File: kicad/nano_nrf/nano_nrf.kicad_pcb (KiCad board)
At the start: 2 copper layers, 50 x 50 mm, 6 parts, among them P1 Digital, P2 Analog, P3 CONN_02X04, P4 CONN_1, P5 CONN_1, P6 CONN_1

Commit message: Leds
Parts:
- added D1: LED, LEDs:LED-5MM, F.Cu at (130.8, 95.2)
- added D2: LED, LEDs:LED-5MM, F.Cu at (162.6, 95.2)
- added D3: LED_RCBG, LEDs:LED-RGB-5MM_Common_Cathode, F.Cu at (143.5, 69.8)
- added R1: 100R, Resistors_ThroughHole:Resistor_Horizontal_RM10mm, F.Cu at (129.5, 88.9)
- added R2: 100R, Resistors_ThroughHole:Resistor_Horizontal_RM10mm, F.Cu at (149.9, 88.9)
- added R3: 180R, Resistors_ThroughHole:Resistor_Horizontal_RM10mm, F.Cu at (133.3, 88.9)
- added R4: 100R, Resistors_ThroughHole:Resistor_Horizontal_RM10mm, F.Cu at (146.1, 88.9)
- added R5: 100R, Resistors_ThroughHole:Resistor_Horizontal_RM10mm, F.Cu at (142.2, 88.9)
- P3: moved to F.Cu
- P4, P5: value CONN_1 -> CONN_01X06; footprint Socket_Arduino_Nano:1pin_Nano -> Socket_Strips:Socket_Strip_Straight_1x06
- moved P5 40.5 mm to (121.9, 88.9), turned to 90 degrees
- moved P4 18.0 mm to (121.9, 106.7), turned to 90 degrees
- moved P3 16.5 mm to (158.8, 86.4)
- moved P1 0.28 mm to (138.4, 76.2)
- moved P2 0.28 mm to (153.7, 76.2)
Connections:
- net /0(Rx) renamed Net-(P1-Pad2)
- net /1(Tx) renamed Net-(P1-Pad1)
- net /2 renamed Net-(P1-Pad5)
- net /4 renamed Net-(P1-Pad7)
- net /A1 renamed Net-(P2-Pad11)
- net /A2 renamed Net-(P2-Pad10)
- net /A3 renamed Net-(P2-Pad9)
- net /A6 renamed Net-(P2-Pad6)
- net /A7 renamed Net-(P2-Pad5)
- net /AREF renamed Net-(P2-Pad13)
- net /Vin renamed Net-(P2-Pad1)
- P1 pad 10: /7 -> Net-(P1-Pad10)
- P1 pad 12: /9(**) -> /9
- P1 pad 13: /10(**/SS) -> /10(SS)
- P1 pad 3: /Reset -> Net-(P1-Pad3)
- P1 pad 6: /3(**) -> /3
- P1 pad 8: /5(**) -> /5
- P1 pad 9: /6(**) -> /6
- P2 pad 14: +3.3V -> /3V3
- P2 pad 3: /Reset -> Net-(P2-Pad3)
- P2 pad 4: +5V -> /5V
- P2 pad 7: /A5 -> /A5(SCL)
- P2 pad 8: /A4 -> /A4(SDA)
- P3 pad 2: +3.3V -> /3V3

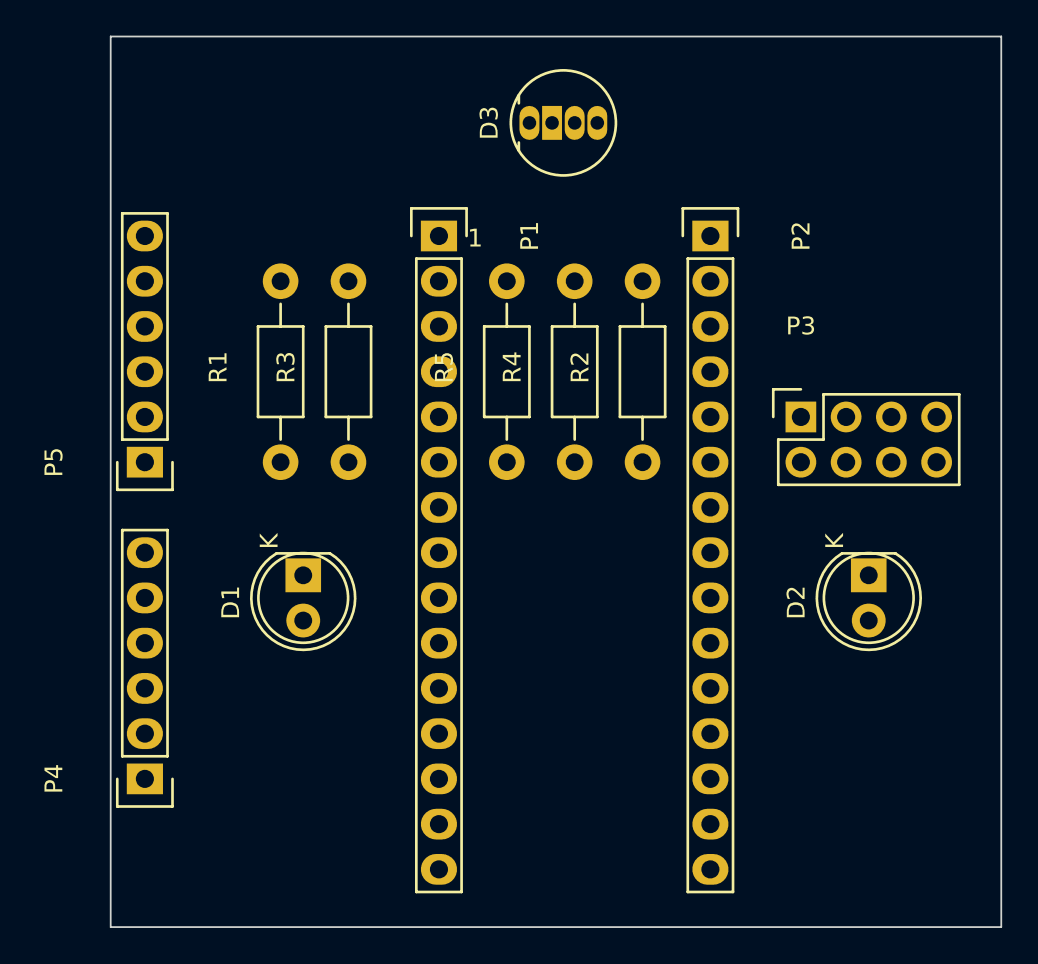
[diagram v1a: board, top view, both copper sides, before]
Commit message: Nano on the bottom
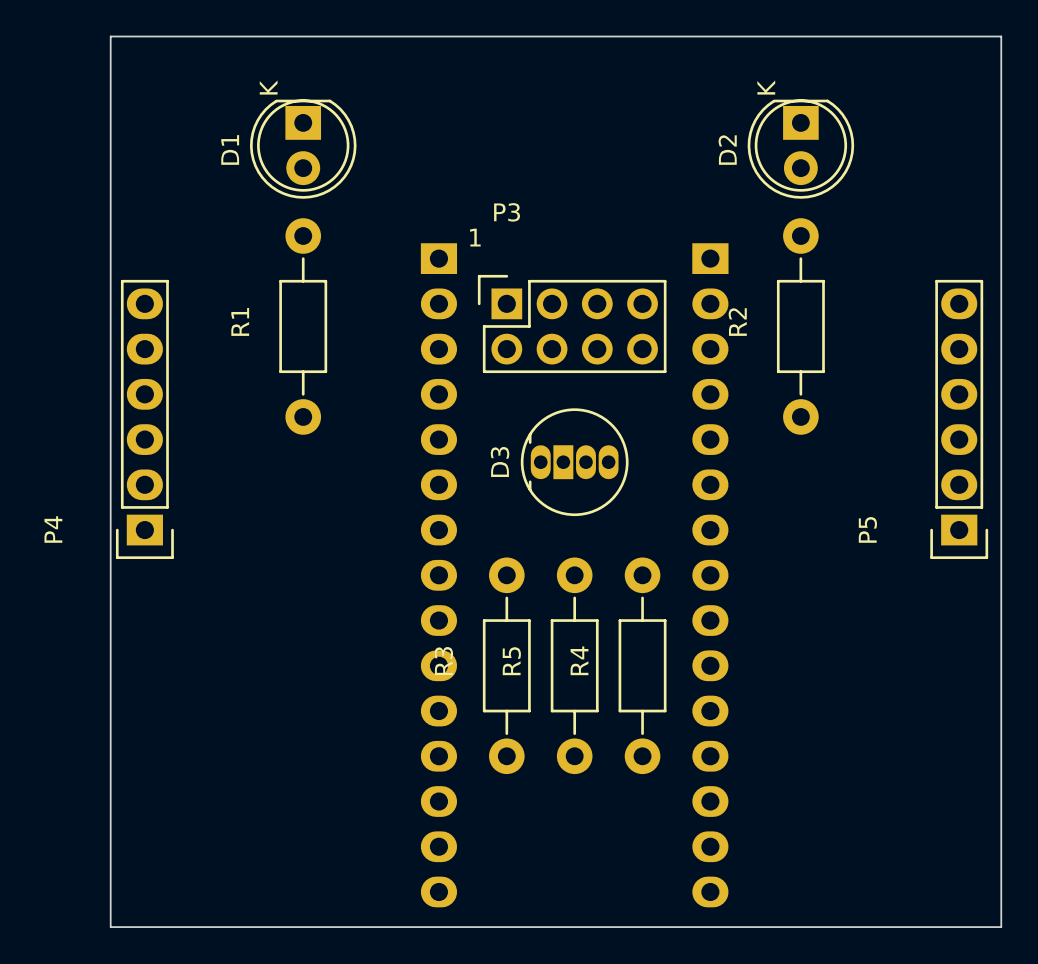
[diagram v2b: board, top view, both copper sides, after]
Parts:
- P1, P2: moved to B.Cu
- moved P5 45.9 mm to (167.6, 92.7)
- moved D2 25.7 mm to (158.8, 69.8)
- moved D1 25.4 mm to (130.8, 69.8)
- moved D3 19.1 mm to (144.1, 88.9)
- moved R3 18.8 mm to (142.2, 105.4)
- moved P3 17.7 mm to (142.2, 80.0)
- moved R4 16.9 mm to (149.9, 105.4)
- moved R5 16.9 mm to (146.1, 105.4)
- moved P1 15.3 mm to (153.7, 77.5)
- moved P2 15.3 mm to (138.4, 77.5)
- moved P4 14.0 mm to (121.9, 92.7)
- moved R2 9.25 mm to (158.8, 86.4)
- moved R1 2.84 mm to (130.8, 86.4)
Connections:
- P1 pad 14: /11(MISO) -> /11(MOSI)
- P1 pad 15: /12(MOSI) -> /12(MISO)
- P3 pad 6: /12(MOSI) -> /11(MOSI)
- P3 pad 7: /11(MISO) -> /12(MISO)
- P5 pad 2: /11(MISO) -> /11(MOSI)
- P5 pad 3: /12(MOSI) -> /12(MISO)

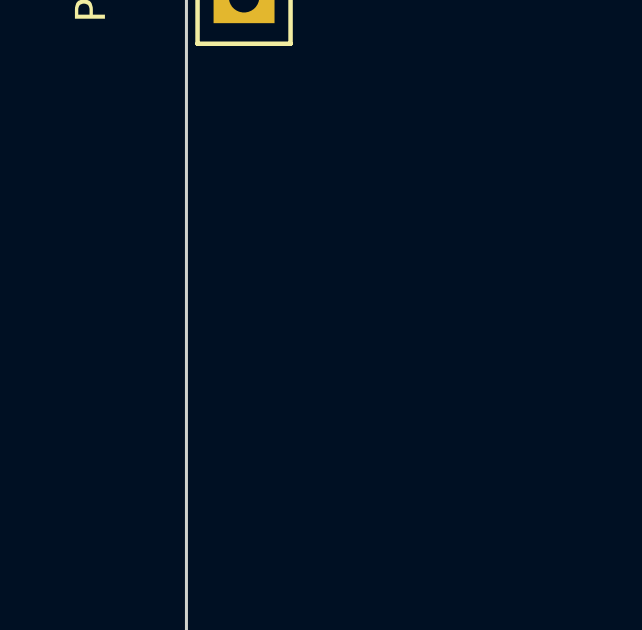
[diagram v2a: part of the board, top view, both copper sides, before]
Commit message: Swap SDA & SCL
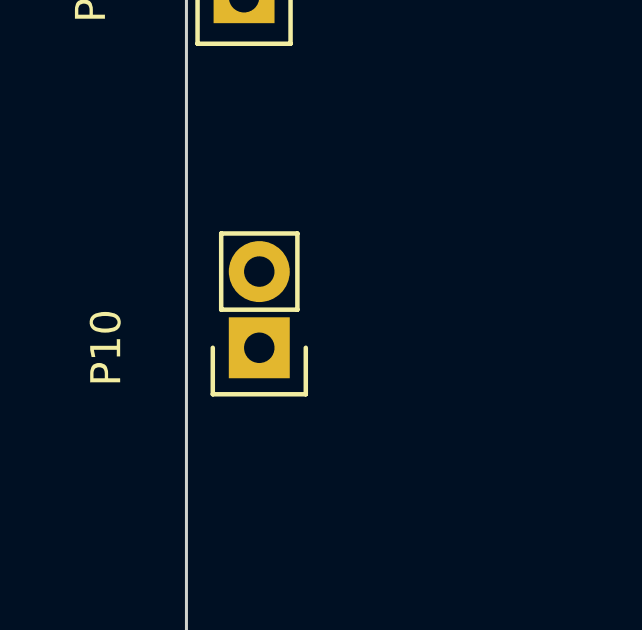
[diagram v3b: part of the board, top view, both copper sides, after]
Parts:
- added P10: CONN_01X02, Socket_Strips:Socket_Strip_Straight_1x02, F.Cu at (122.4, 104.4)
- P6: value CONN_1 -> CONN_01X02
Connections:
- P2 pad 11: Net-(P2-Pad11) -> /A1
- P4 pad 1: /A0 -> GND
- P4 pad 2: /A4(SDA) -> /3V3
- P4 pad 4: /5V -> /A4(SDA)
- P4 pad 5: /3V3 -> /A1
- P4 pad 6: GND -> /A0
- P5 pad 1: /10(SS) -> GND
- P5 pad 2: /11(MOSI) -> /3V3
- P5 pad 3: /12(MISO) -> /13(SCK)
- P5 pad 4: /13(SCK) -> /12(MISO)
- P5 pad 5: /3V3 -> /11(MOSI)
- P5 pad 6: GND -> /10(SS)
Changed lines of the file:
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@@
-(kicad_pcb (version 4) (host pcbnew 4.0.2-4+6225~38~ubuntu14.04.1-stable)
+(kicad_pcb (version 4) (host pcbnew 4.0.1-stable)
   (general
-    (links 32)
-    (no_connects 32)
+    (links 34)
+    (no_connects 34)
     (area 119.949999 64.949999 170.050001 115.050001)
     (thickness 1.6)
@@
     (tracks 0)
     (zones 0)
-    (modules 14)
+    (modules 15)
     (nets 37)
   )
@@
     (pad_to_mask_clearance 0)
     (aux_axis_origin 138.176 110.617)
-    (visible_elements FFFFF77F)
+    (visible_elements 7FFFFFFF)
     (pcbplotparams
       (layerselection 0x00030_80000001)
@@
   (net 30 "Net-(P2-Pad9)")
   (net 31 "Net-(P2-Pad10)")
-  (net 32 "Net-(P2-Pad11)")
-  (net 33 "Net-(P2-Pad13)")
-  (net 34 /3V3)
-  (net 35 "/11(MOSI)")
-  (net 36 "/12(MISO)")
+  (net 32 "Net-(P2-Pad13)")
+  (net 33 /3V3)
+  (net 34 "/11(MOSI)")
+  (net 35 "/12(MISO)")
+  (net 36 /A1)
   (net_class Default "This is the default net class."
     (clearance 0.2)
@@
     (add_net /9)
     (add_net /A0)
+    (add_net /A1)
     (add_net "/A4(SDA)")
     (add_net "/A5(SCL)")
@@
     (add_net "Net-(P2-Pad1)")
     (add_net "Net-(P2-Pad10)")
-    (add_net "Net-(P2-Pad11)")
     (add_net "Net-(P2-Pad13)")
     (add_net "Net-(P2-Pad3)")
@@
       (effects (font (size 1 1) (thickness 0.15)))
     )
-    (fp_text value CONN_1 (at 0 2.032) (layer F.Fab) hide
+    (fp_text value CONN_01X02 (at 0 2.032) (layer F.Fab) hide
       (effects (font (size 1 1) (thickness 0.15)))
     )
@@
       (net 1 GND))
     (pad 2 thru_hole oval (at 0 2.54) (size 1.7272 1.7272) (drill 1.016) (layers *.Cu *.Mask F.SilkS)
-      (net 34 /3V3))
+      (net 33 /3V3))
     (pad 3 thru_hole oval (at 2.54 0) (size 1.7272 1.7272) (drill 1.016) (layers *.Cu *.Mask F.SilkS)
       (net 2 /7))
@@
       (net 5 "/13(SCK)"))
     (pad 6 thru_hole oval (at 5.08 2.54) (size 1.7272 1.7272) (drill 1.016) (layers *.Cu *.Mask F.SilkS)
-      (net 35 "/11(MOSI)"))
+      (net 34 "/11(MOSI)"))
     (pad 7 thru_hole oval (at 7.62 0) (size 1.7272 1.7272) (drill 1.016) (layers *.Cu *.Mask F.SilkS)
-      (net 36 "/12(MISO)"))
+      (net 35 "/12(MISO)"))
     (pad 8 thru_hole oval (at 7.62 2.54) (size 1.7272 1.7272) (drill 1.016) (layers *.Cu *.Mask F.SilkS)
       (net 6 "Net-(P3-Pad8)"))
@@
       (net 22 "/10(SS)"))
     (pad 14 thru_hole oval (at 33.02 0 270) (size 1.7272 2.032) (drill 1.016) (layers *.Cu *.Mask B.SilkS)
-      (net 35 "/11(MOSI)"))
+      (net 34 "/11(MOSI)"))
     (pad 15 thru_hole oval (at 35.56 0 270) (size 1.7272 2.032) (drill 1.016) (layers *.Cu *.Mask B.SilkS)
-      (net 36 "/12(MISO)"))
+      (net 35 "/12(MISO)"))
     (model Socket_Strips.3dshapes/Socket_Strip_Straight_1x15.wrl
       (at (xyz 0.7 0 0))
@@
       (net 31 "Net-(P2-Pad10)"))
     (pad 11 thru_hole oval (at 25.4 0 270) (size 1.7272 2.032) (drill 1.016) (layers *.Cu *.Mask B.SilkS)
-      (net 32 "Net-(P2-Pad11)"))
+      (net 36 /A1))
     (pad 12 thru_hole oval (at 27.94 0 270) (size 1.7272 2.032) (drill 1.016) (layers *.Cu *.Mask B.SilkS)
       (net 4 /A0))
     (pad 13 thru_hole oval (at 30.48 0 270) (size 1.7272 2.032) (drill 1.016) (layers *.Cu *.Mask B.SilkS)
-      (net 33 "Net-(P2-Pad13)"))
+      (net 32 "Net-(P2-Pad13)"))
     (pad 14 thru_hole oval (at 33.02 0 270) (size 1.7272 2.032) (drill 1.016) (layers *.Cu *.Mask B.SilkS)
-      (net 34 /3V3))
+      (net 33 /3V3))
     (pad 15 thru_hole oval (at 35.56 0 270) (size 1.7272 2.032) (drill 1.016) (layers *.Cu *.Mask B.SilkS)
       (net 5 "/13(SCK)"))
@@
     (fp_line (start -1.55 -1.55) (end -1.55 1.55) (layer F.SilkS) (width 0.15))
     (pad 1 thru_hole rect (at 0 0 90) (size 1.7272 2.032) (drill 1.016) (layers *.Cu *.Mask F.SilkS)
-      (net 4 /A0))
+      (net 1 GND))
     (pad 2 thru_hole oval (at 2.54 0 90) (size 1.7272 2.032) (drill 1.016) (layers *.Cu *.Mask F.SilkS)
-      (net 29 "/A4(SDA)"))
+      (net 33 /3V3))
     (pad 3 thru_hole oval (at 5.08 0 90) (size 1.7272 2.032) (drill 1.016) (layers *.Cu *.Mask F.SilkS)
       (net 28 "/A5(SCL)"))
     (pad 4 thru_hole oval (at 7.62 0 90) (size 1.7272 2.032) (drill 1.016) (layers *.Cu *.Mask F.SilkS)
-      (net 25 /5V))
+      (net 29 "/A4(SDA)"))
     (pad 5 thru_hole oval (at 10.16 0 90) (size 1.7272 2.032) (drill 1.016) (layers *.Cu *.Mask F.SilkS)
-      (net 34 /3V3))
+      (net 36 /A1))
     (pad 6 thru_hole oval (at 12.7 0 90) (size 1.7272 2.032) (drill 1.016) (layers *.Cu *.Mask F.SilkS)
-      (net 1 GND))
+      (net 4 /A0))
     (model Socket_Strips.3dshapes/Socket_Strip_Straight_1x06.wrl
       (at (xyz 0.25 0 0))
@@
     (fp_line (start -1.55 -1.55) (end -1.55 1.55) (layer F.SilkS) (width 0.15))
     (pad 1 thru_hole rect (at 0 0 90) (size 1.7272 2.032) (drill 1.016) (layers *.Cu *.Mask F.SilkS)
+      (net 1 GND))
+    (pad 2 thru_hole oval (at 2.54 0 90) (size 1.7272 2.032) (drill 1.016) (layers *.Cu *.Mask F.SilkS)
+      (net 33 /3V3))
+    (pad 3 thru_hole oval (at 5.08 0 90) (size 1.7272 2.032) (drill 1.016) (layers *.Cu *.Mask F.SilkS)
+      (net 5 "/13(SCK)"))
+    (pad 4 thru_hole oval (at 7.62 0 90) (size 1.7272 2.032) (drill 1.016) (layers *.Cu *.Mask F.SilkS)
+      (net 35 "/12(MISO)"))
+    (pad 5 thru_hole oval (at 10.16 0 90) (size 1.7272 2.032) (drill 1.016) (layers *.Cu *.Mask F.SilkS)
+      (net 34 "/11(MOSI)"))
+    (pad 6 thru_hole oval (at 12.7 0 90) (size 1.7272 2.032) (drill 1.016) (layers *.Cu *.Mask F.SilkS)
       (net 22 "/10(SS)"))
-    (pad 2 thru_hole oval (at 2.54 0 90) (size 1.7272 2.032) (drill 1.016) (layers *.Cu *.Mask F.SilkS)
-      (net 35 "/11(MOSI)"))
-    (pad 3 thru_hole oval (at 5.08 0 90) (size 1.7272 2.032) (drill 1.016) (layers *.Cu *.Mask F.SilkS)
-      (net 36 "/12(MISO)"))
-    (pad 4 thru_hole oval (at 7.62 0 90) (size 1.7272 2.032) (drill 1.016) (layers *.Cu *.Mask F.SilkS)
-      (net 5 "/13(SCK)"))
-    (pad 5 thru_hole oval (at 10.16 0 90) (size 1.7272 2.032) (drill 1.016) (layers *.Cu *.Mask F.SilkS)
-      (net 34 /3V3))
-    (pad 6 thru_hole oval (at 12.7 0 90) (size 1.7272 2.032) (drill 1.016) (layers *.Cu *.Mask F.SilkS)
-      (net 1 GND))
     (model Socket_Strips.3dshapes/Socket_Strip_Straight_1x06.wrl
       (at (xyz 0.25 0 0))
@@
     )
   )
+  (module Socket_Strips:Socket_Strip_Straight_1x02 (layer F.Cu)
+    (at 122.428 104.394 90)
+    (descr "Through hole socket strip")
+    (tags "socket strip")
+    (fp_text reference P10 (at 0 -5.1 90) (layer F.SilkS)
+      (effects (font (size 1 1) (thickness 0.15)))
+    )
+    (fp_text value CONN_01X02 (at 0 -3.1 90) (layer F.Fab)
+      (effects (font (size 1 1) (thickness 0.15)))
+    )
+    (fp_line (start -1.55 1.55) (end 0 1.55) (layer F.SilkS) (width 0.15))
+    (fp_line (start 3.81 1.27) (end 1.27 1.27) (layer F.SilkS) (width 0.15))
+    (fp_line (start -1.75 -1.75) (end -1.75 1.75) (layer F.CrtYd) (width 0.05))
+    (fp_line (start 4.3 -1.75) (end 4.3 1.75) (layer F.CrtYd) (width 0.05))
+    (fp_line (start -1.75 -1.75) (end 4.3 -1.75) (layer F.CrtYd) (width 0.05))
+    (fp_line (start -1.75 1.75) (end 4.3 1.75) (layer F.CrtYd) (width 0.05))
+    (fp_line (start 1.27 1.27) (end 1.27 -1.27) (layer F.SilkS) (width 0.15))
+    (fp_line (start 0 -1.55) (end -1.55 -1.55) (layer F.SilkS) (width 0.15))
+    (fp_line (start -1.55 -1.55) (end -1.55 1.55) (layer F.SilkS) (width 0.15))
+    (fp_line (start 1.27 -1.27) (end 3.81 -1.27) (layer F.SilkS) (width 0.15))
+    (fp_line (start 3.81 -1.27) (end 3.81 1.27) (layer F.SilkS) (width 0.15))
+    (pad 1 thru_hole rect (at 0 0 90) (size 2.032 2.032) (drill 1.016) (layers *.Cu *.Mask F.SilkS)
+      (net 1 GND))
+    (pad 2 thru_hole oval (at 2.54 0 90) (size 2.032 2.032) (drill 1.016) (layers *.Cu *.Mask F.SilkS)
+      (net 25 /5V))
+    (model Socket_Strips.3dshapes/Socket_Strip_Straight_1x02.wrl
+      (at (xyz 0.05 0 0))
+      (scale (xyz 1 1 1))
+      (rotate (xyz 0 0 180))
+    )
+  )
